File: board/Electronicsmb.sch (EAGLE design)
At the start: 37 parts

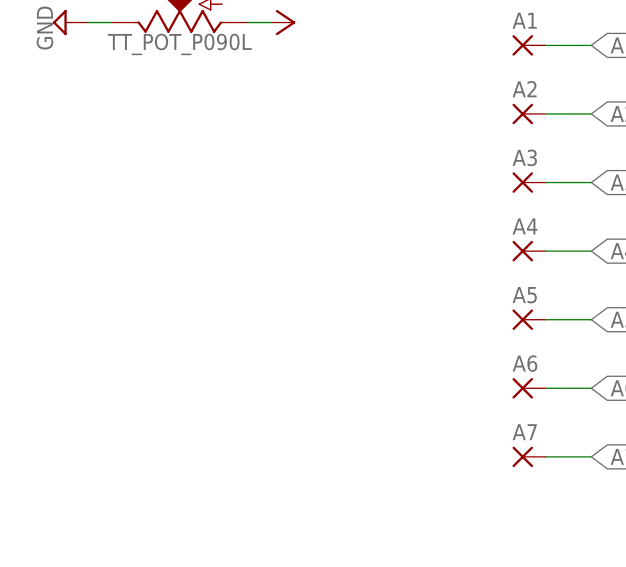
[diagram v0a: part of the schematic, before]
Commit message: larger drill holes and points for positive and negative
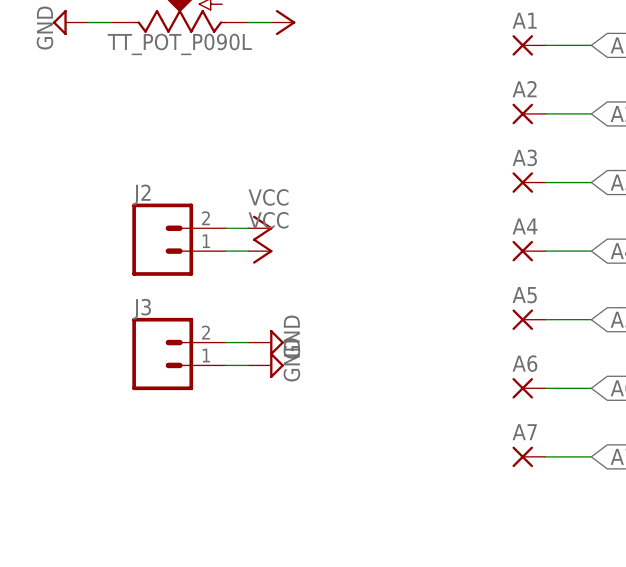
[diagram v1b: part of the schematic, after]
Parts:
- added J2, J3: (no value), SparkFun-Connectors:CONN_02
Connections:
- net GND: now also J3.1, J3.2
- net VCC: now also J2.1, J2.2
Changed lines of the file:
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@@
 <part name="R2" library="resistor" library_urn="urn:adsk.eagle:library:348" deviceset="R-US_" device="0204/7" package3d_urn="urn:adsk.eagle:package:25945/1" value="270"/>
 <part name="SUPPLY1" library="supply2" library_urn="urn:adsk.eagle:library:372" deviceset="GND" device=""/>
+<part name="J2" library="SparkFun-Connectors" library_urn="urn:adsk.eagle:library:513" deviceset="CONN_02" device="" package3d_urn="urn:adsk.eagle:package:38039/1"/>
+<part name="J3" library="SparkFun-Connectors" library_urn="urn:adsk.eagle:library:513" deviceset="CONN_02" device="" package3d_urn="urn:adsk.eagle:package:38039/1"/>
+<part name="P+4" library="supply1" library_urn="urn:adsk.eagle:library:371" deviceset="VCC" device=""/>
+<part name="P+5" library="supply1" library_urn="urn:adsk.eagle:library:371" deviceset="VCC" device=""/>
+<part name="SUPPLY7" library="supply2" library_urn="urn:adsk.eagle:library:372" deviceset="GND" device=""/>
+<part name="SUPPLY8" library="supply2" library_urn="urn:adsk.eagle:library:372" deviceset="GND" device=""/>
 </parts>
 <sheets>
@@
 <instance part="R2" gate="G$1" x="185.42" y="55.88"/>
 <instance part="SUPPLY1" gate="GND" x="139.7" y="93.98" rot="R90"/>
+<instance part="J2" gate="G$1" x="35.56" y="43.18"/>
+<instance part="J3" gate="G$1" x="35.56" y="30.48"/>
+<instance part="P+4" gate="VCC" x="48.26" y="45.72" rot="R270"/>
+<instance part="P+5" gate="VCC" x="48.26" y="43.18" rot="R270"/>
+<instance part="SUPPLY7" gate="GND" x="48.26" y="33.02" rot="R90"/>
+<instance part="SUPPLY8" gate="GND" x="48.26" y="30.48" rot="R90"/>
 </instances>
 <busses>
@@
 <wire x1="134.62" y1="93.98" x2="137.16" y2="93.98" width="0.1524" layer="91"/>
 </segment>
+<segment>
+<pinref part="J3" gate="G$1" pin="2"/>
+<pinref part="SUPPLY7" gate="GND" pin="GND"/>
+<wire x1="43.18" y1="33.02" x2="45.72" y2="33.02" width="0.1524" layer="91"/>
+</segment>
+<segment>
+<pinref part="J3" gate="G$1" pin="1"/>
+<pinref part="SUPPLY8" gate="GND" pin="GND"/>
+<wire x1="43.18" y1="30.48" x2="45.72" y2="30.48" width="0.1524" layer="91"/>
+</segment>
 </net>
 <net name="VCC" class="0">
@@
 <wire x1="30.48" y1="134.62" x2="33.02" y2="134.62" width="0.1524" layer="91"/>
 </segment>
+<segment>
+<pinref part="J2" gate="G$1" pin="2"/>
+<pinref part="P+4" gate="VCC" pin="VCC"/>
+<wire x1="43.18" y1="45.72" x2="45.72" y2="45.72" width="0.1524" layer="91"/>
+</segment>
+<segment>
+<pinref part="J2" gate="G$1" pin="1"/>
+<pinref part="P+5" gate="VCC" pin="VCC"/>
+<wire x1="43.18" y1="43.18" x2="45.72" y2="43.18" width="0.1524" layer="91"/>
+</segment>
 </net>

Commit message: minor tweaks
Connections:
- new net RAW: J1.2, U$1.RAW
- net VCC: no longer J1.2
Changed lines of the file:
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@@
 <part name="P+1" library="supply1" library_urn="urn:adsk.eagle:library:371" deviceset="VCC" device=""/>
 <part name="J1" library="SparkFun-Connectors" library_urn="urn:adsk.eagle:library:513" deviceset="CONN_02" device="" package3d_urn="urn:adsk.eagle:package:38039/1"/>
-<part name="P+3" library="supply1" library_urn="urn:adsk.eagle:library:371" deviceset="VCC" device=""/>
 <part name="SUPPLY3" library="supply2" library_urn="urn:adsk.eagle:library:372" deviceset="GND" device=""/>
 <part name="A1" library="wirepad" deviceset="2,54/1,0" device=""/>
@@
 <instance part="P+1" gate="VCC" x="50.8" y="68.58" rot="R270"/>
 <instance part="J1" gate="G$1" x="22.86" y="132.08"/>
-<instance part="P+3" gate="VCC" x="35.56" y="134.62" rot="R270"/>
 <instance part="SUPPLY3" gate="GND" x="35.56" y="132.08" rot="R90"/>
 <instance part="A1" gate="P" x="76.2" y="66.04"/>
@@
 </segment>
 <segment>
-<pinref part="J1" gate="G$1" pin="2"/>
-<pinref part="P+3" gate="VCC" pin="VCC"/>
-<wire x1="30.48" y1="134.62" x2="33.02" y2="134.62" width="0.1524" layer="91"/>
-</segment>
-<segment>
 <pinref part="J2" gate="G$1" pin="2"/>
 <pinref part="P+4" gate="VCC" pin="VCC"/>
@@
 </segment>
 </net>
+<net name="RAW" class="0">
+<segment>
+<pinref part="U$1" gate="G$1" pin="RAW"/>
+<wire x1="78.74" y1="93.98" x2="73.66" y2="93.98" width="0.1524" layer="91"/>
+<label x="73.66" y="88.9" size="1.778" layer="95"/>
+</segment>
+<segment>
+<pinref part="J1" gate="G$1" pin="2"/>
+<wire x1="30.48" y1="134.62" x2="33.02" y2="134.62" width="0.1524" layer="91"/>
+<label x="35.56" y="134.62" size="1.778" layer="95"/>
+</segment>
+</net>

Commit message: final tweaks to V1 and starter code
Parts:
- removed A1, A2, A3: (no value), wirepad:2,54/1,0
- added J4: (no value), SparkFun-Connectors:CONN_04
- R1, R10, R11, R12, R13, R14, R2, R3, R4, R6, R7, R8, R9: device resistor:R-US_0204/7 -> SparkFun:RESISTORPTH-1/4W
- renumbered D1 to D15, D13 to D16
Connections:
- removed net D1: R14.1, U$1.RX1
- removed net N$1: S1.S, U$1.TX0
- new net RX: J4.2, U$1.RX1
- new net TX: J4.3, U$1.TX0
- net A1: now also R14.1; no longer A1.P
- net A2: now also R2.1; no longer A2.P
- net A3: now also S1.S; no longer A3.P
- net D13: no longer R2.1
- net GND: now also J4.1
- net VCC: now also J4.4
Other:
- moved on the sheet: S1
